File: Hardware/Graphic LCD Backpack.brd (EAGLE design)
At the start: 51.4 x 28.2 mm, 27 parts, among them Q1 TRANSISTOR_PNPSMD, U1 V_REG_LDOSMD, U2 ATMEGA168, Y1 RESONATORSMD

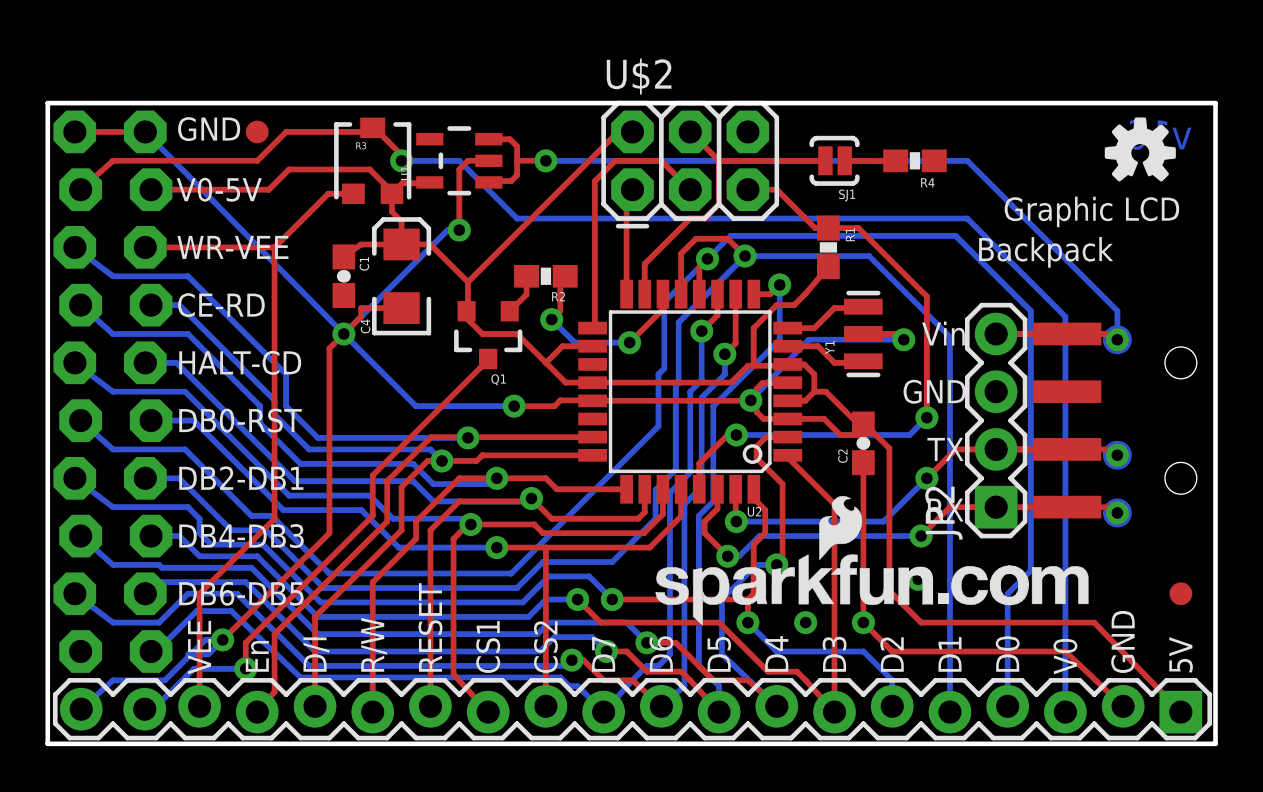
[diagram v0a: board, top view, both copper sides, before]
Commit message: Update label placements
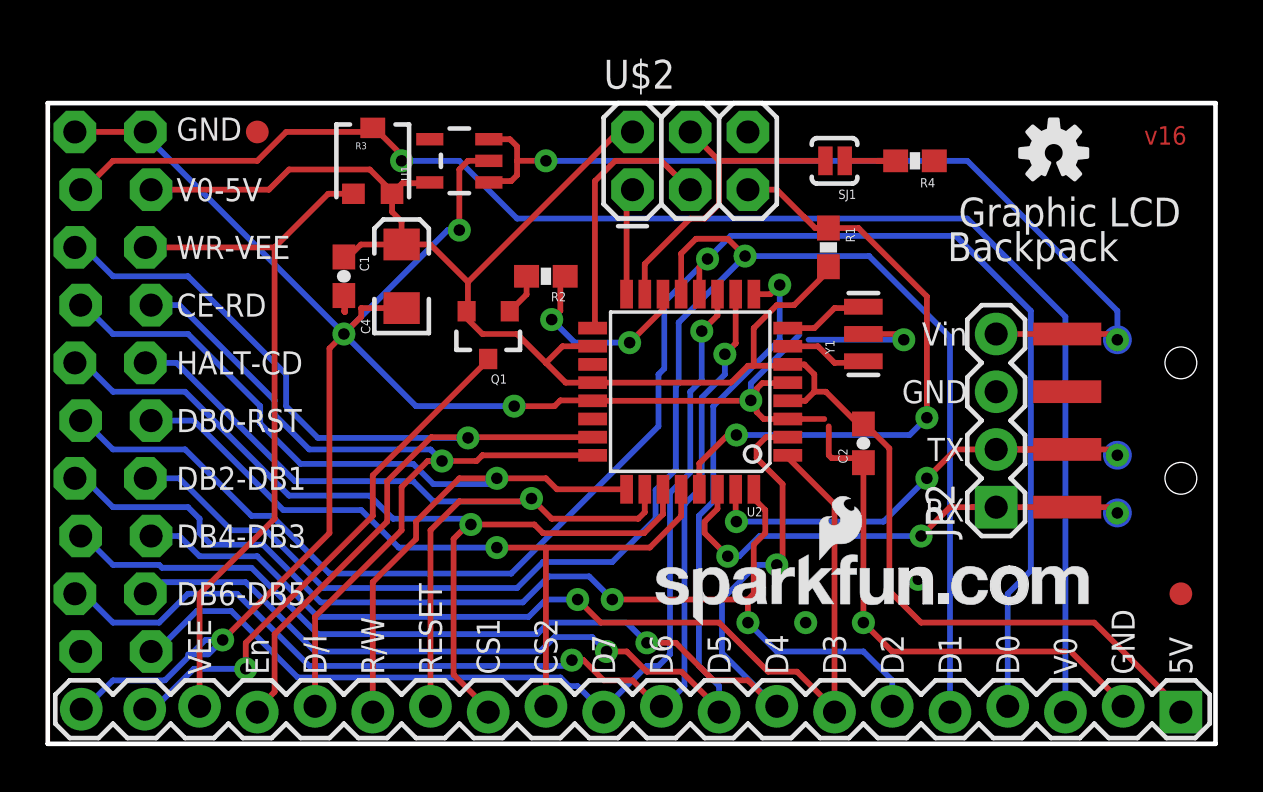
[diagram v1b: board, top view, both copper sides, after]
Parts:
- moved LOGO3 3.81 mm to (44.2, 26.0)
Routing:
- net GND: track 114.5 -> 116.1 mm
